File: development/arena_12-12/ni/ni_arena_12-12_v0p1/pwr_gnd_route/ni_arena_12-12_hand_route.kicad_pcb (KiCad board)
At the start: 6 copper layers, 228.6 x 228.6 mm, 581 parts, among them J1 Barrel_Jack, J2 NI_TE_68pos, J3 Barrel_Jack, P1 CONN15, P10 CONN15, P11 CONN15, P12 CONN15, P2 CONN15, P3 CONN15, P4 CONN15, P5 CONN15, P6 CONN15, P7 CONN15, P8 CONN15, P9 CONN15, Q1 MOSFET_NCHAN, SW1 SW_SPDT, U1 AP2112K-3.3, U10 TXB0108PW, U100 74LVC2G17, U101 74LVC2G17, U102 74LVC2G17, U103 74LVC2G17, U104 74LVC2G17, U105 74LVC2G17, U106 74LVC2G17, U107 74LVC2G17, U108 74LVC2G17, U109 74LVC2G17, U11 TXB0108PW, U110 74LVC2G17, U12 TXB0108PW, U13 TXB0108PW, U14 TXB0108PW, U15 TXB0108PW, U16 TXB0108PW, U17 TXB0108PW, U18 TXB0108PW, U19 74LVC2G17, U2 TXB0108PW, U20 74LVC2G17, U21 74LVC2G17, U22 74LVC2G17, U23 74LVC2G17, U24 74LVC2G17, U25 74LVC2G17, U26 74LVC2G17, U27 74LVC2G17, U28 74LVC2G17, U29 74LVC2G17, U3 TXB0108PW, U30 74LVC2G17, U31 74LVC2G17, U32 74LVC2G17, U33 74LVC2G17, U34 74LVC2G17, U35 74LVC2G17, U36 74LVC2G17, U37 74LVC2G17, U38 74LVC2G17, U39 74LVC2G17, U4 TXB0108PW, U40 74LVC2G17, U41 74LVC2G17, U42 74LVC2G17, U43 74LVC2G17, U44 74LVC2G17, U45 74LVC2G17, U46 74LVC2G17, U47 74LVC2G17, U48 74LVC2G17, U49 74LVC2G17, U5 TXB0108PW, U50 74LVC2G17, U51 74LVC2G17, U52 74LVC2G17, U53 74LVC2G17, U54 74LVC2G17, U55 74LVC2G17, U56 74LVC2G17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

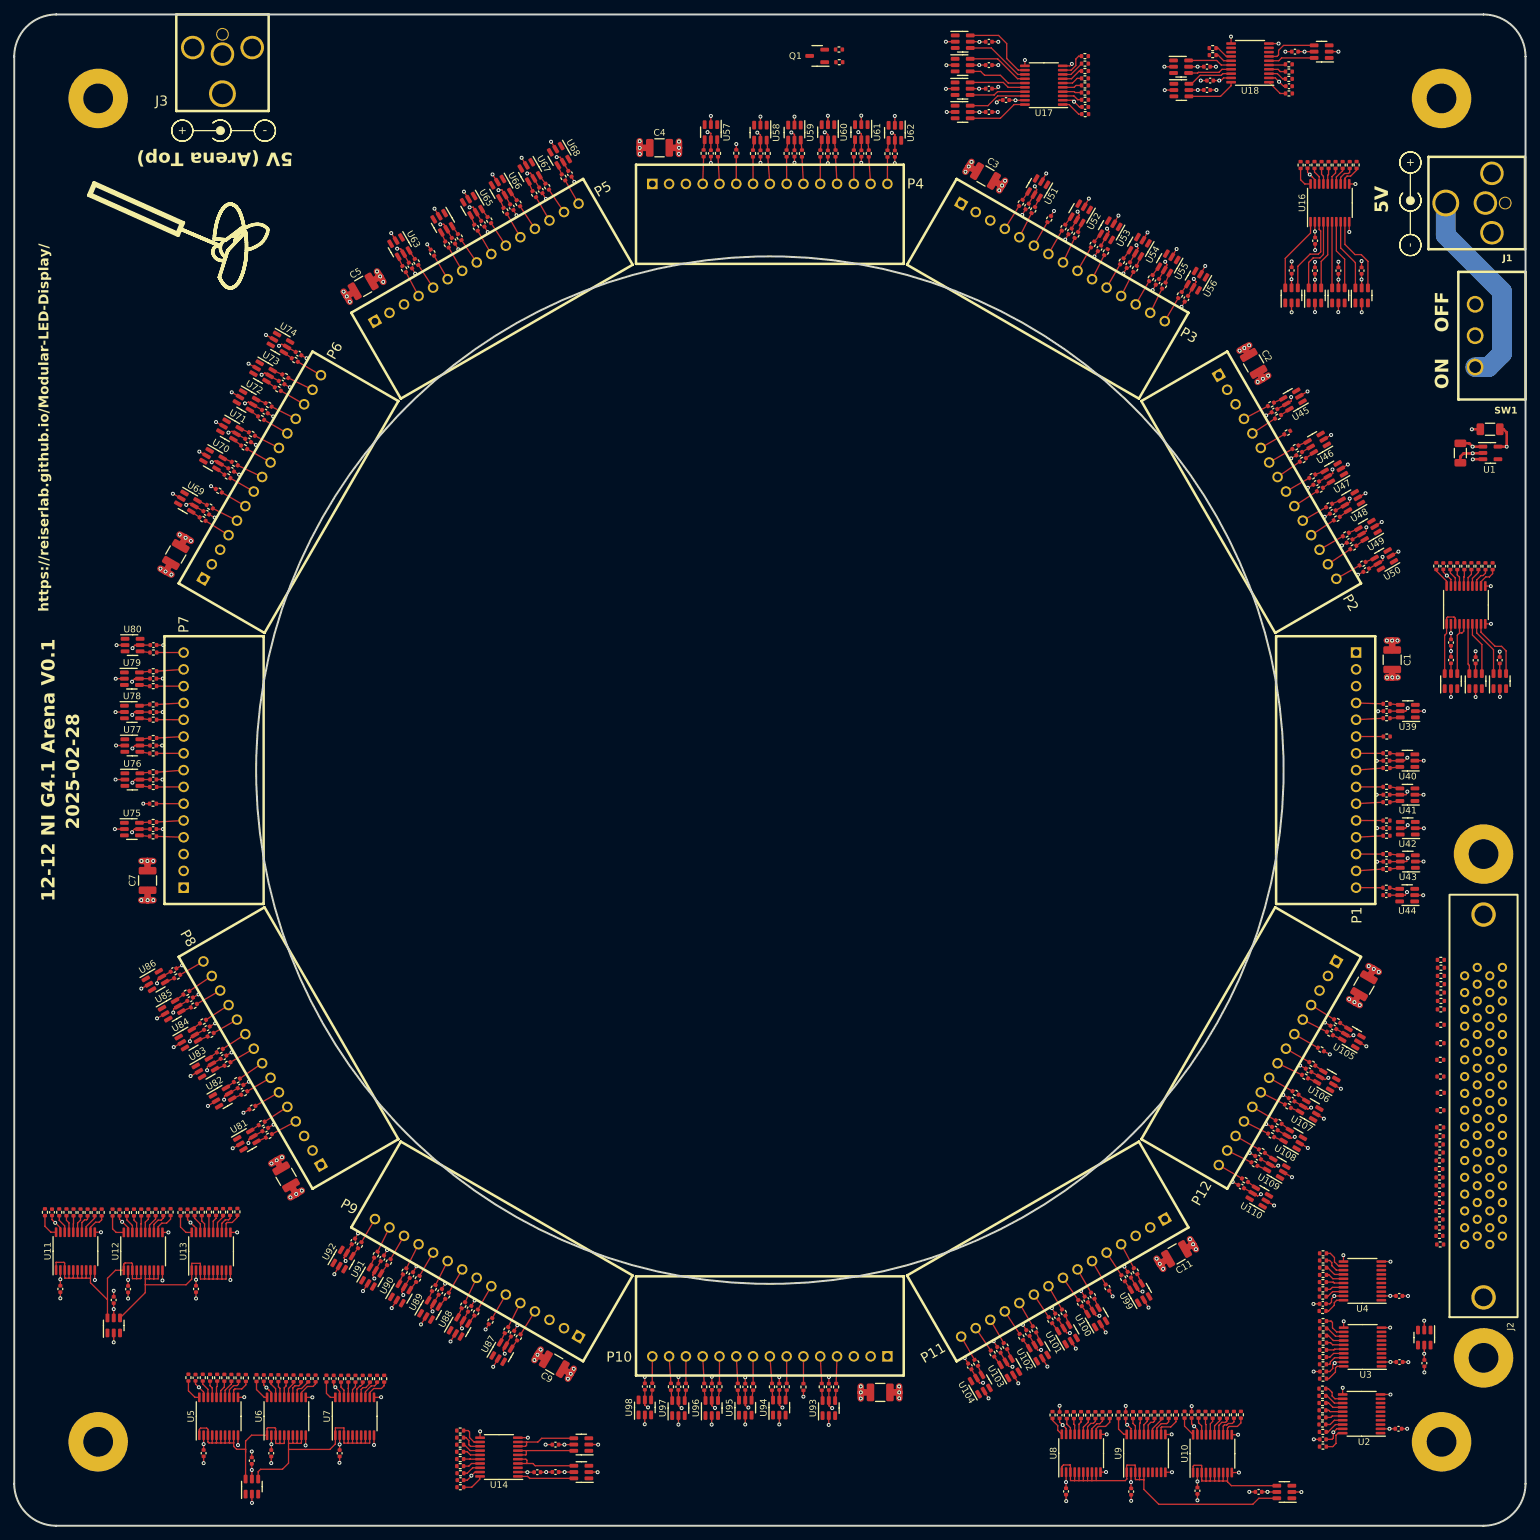
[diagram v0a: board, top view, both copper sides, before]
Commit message: Finished autorouting for new route of NI 12-12 arena which fix hand route.
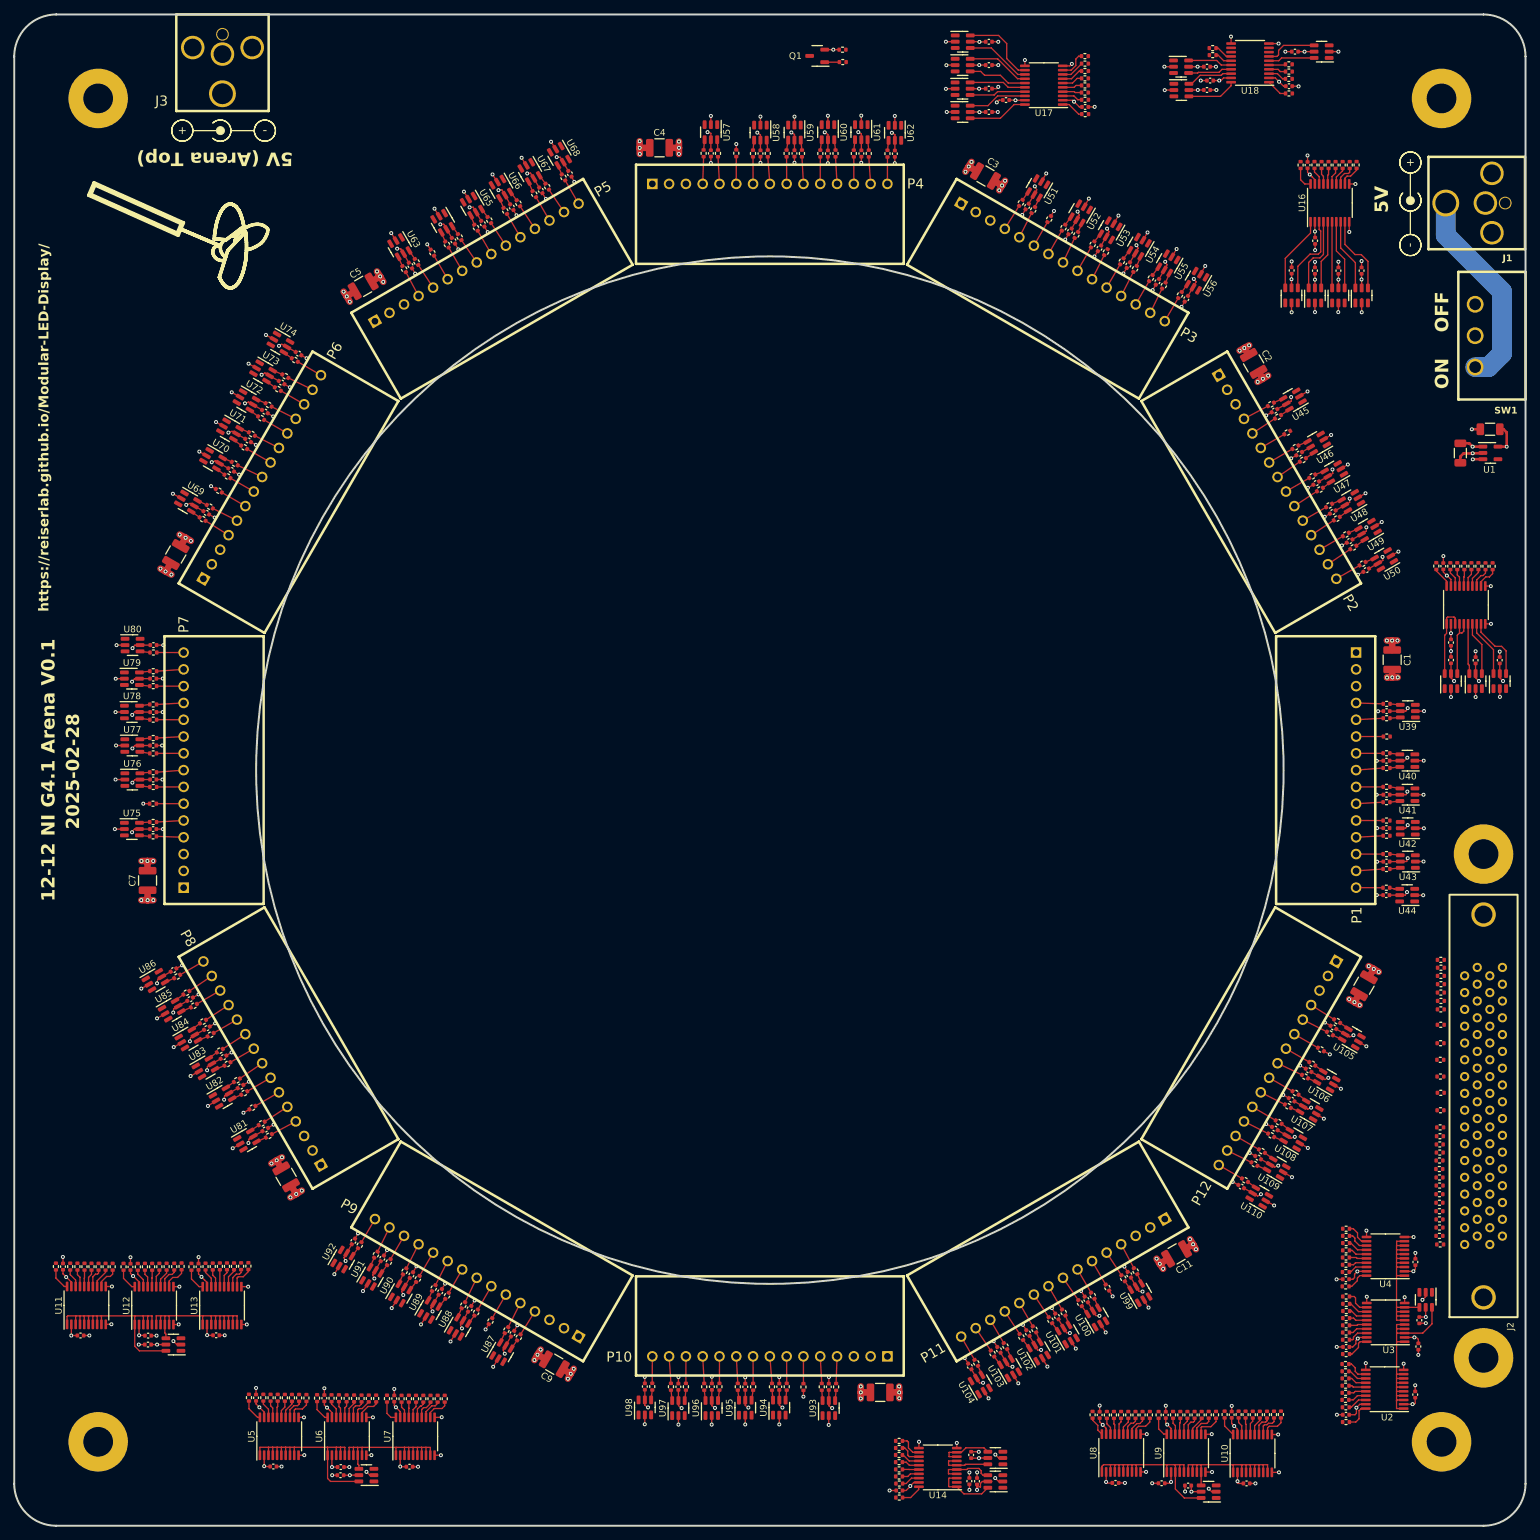
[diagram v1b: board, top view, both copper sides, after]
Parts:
- moved R125 66.4 mm to (197.4, 287.8)
- moved R129 66.4 mm to (197.3, 282.5)
- moved R130 66.4 mm to (197.3, 281.4)
- moved U14 66.4 mm to (203.2, 283.3)
- moved C132 66.4 mm to (197.4, 286.8)
- moved R126 66.4 mm to (197.4, 285.7)
- moved R127 66.4 mm to (197.3, 284.6)
- moved R128 66.4 mm to (197.3, 283.6)
- moved R131 66.4 mm to (197.3, 280.3)
- moved R132 66.4 mm to (197.3, 279.3)
- moved C131 65.4 mm to (208.0, 285.3), turned to 90 degrees
- moved C19 63.8 mm to (209.1, 285.4), turned to 90 degrees
- moved C20 62.9 mm to (208.2, 281.4), turned to 90 degrees
- moved U24 62.7 mm to (211.9, 281.9)
- moved U23 62.6 mm to (211.9, 285.4)
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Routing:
- net Net-(U2-A1): track 0.00 -> 33.5 mm
- net Net-(U3-A5): track 0.00 -> 28.5 mm
- net Net-(U8-A1): track 52.9 -> 32.5 mm
- net GND: track 297.2 -> 309.8 mm, vias 259 -> 273
- net Net-(U6-A5): track 40.6 -> 28.8 mm
- net Net-(U12-A5): track 40.0 -> 30.3 mm
- net Net-(U10-A1): track 24.1 -> 27.7 mm
- net Net-(U14-A5): track 10.3 -> 7.93 mm
- net Net-(U14-A7): track 10.6 -> 8.20 mm
- net Net-(Q1-G): track 0.00 -> 2.23 mm
- net +3.3V: track 98.5 -> 100.5 mm, vias 46 -> 49
- net Net-(U14-A3): track 10.5 -> 8.58 mm
- net Net-(U11-A1): track 37.8 -> 36.6 mm
- net Net-(U14-A1): track 8.61 -> 9.20 mm

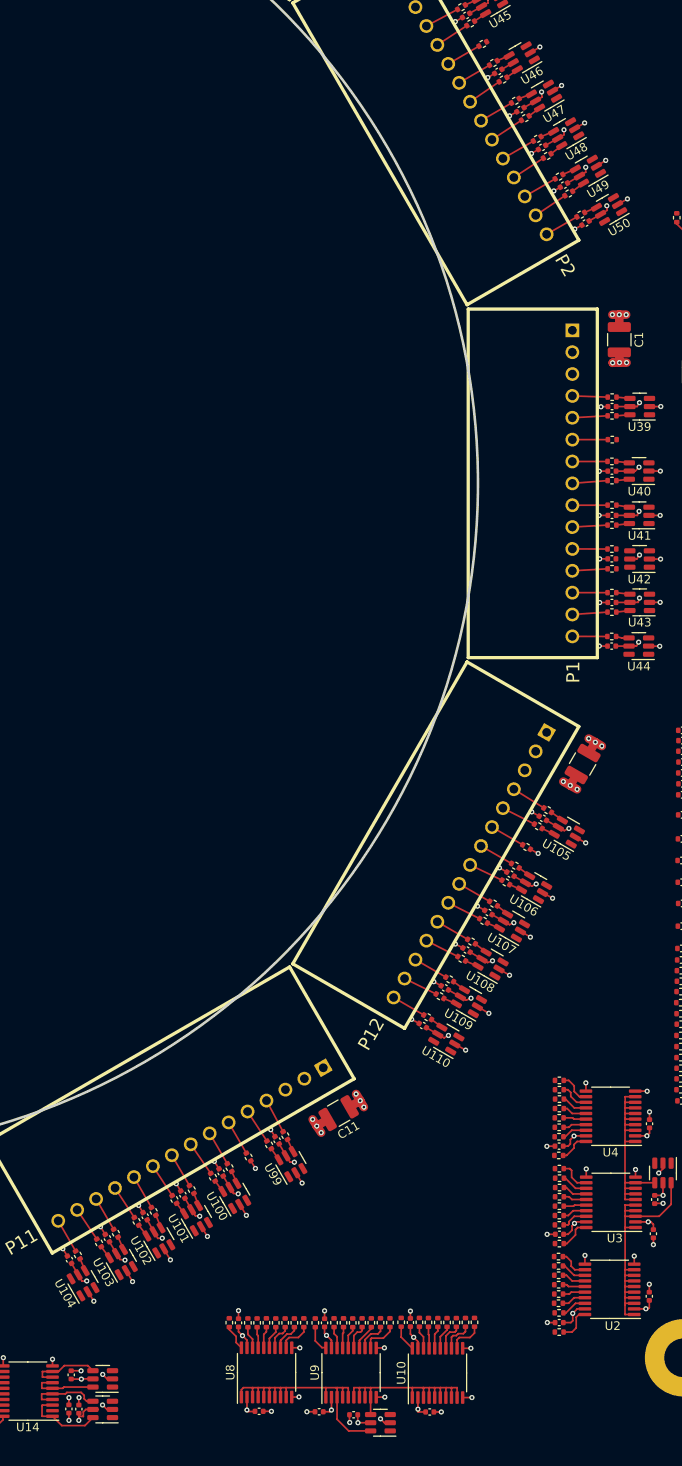
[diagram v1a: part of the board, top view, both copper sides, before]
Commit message: Add new route to NI 12-12 .kicad_pcb file.
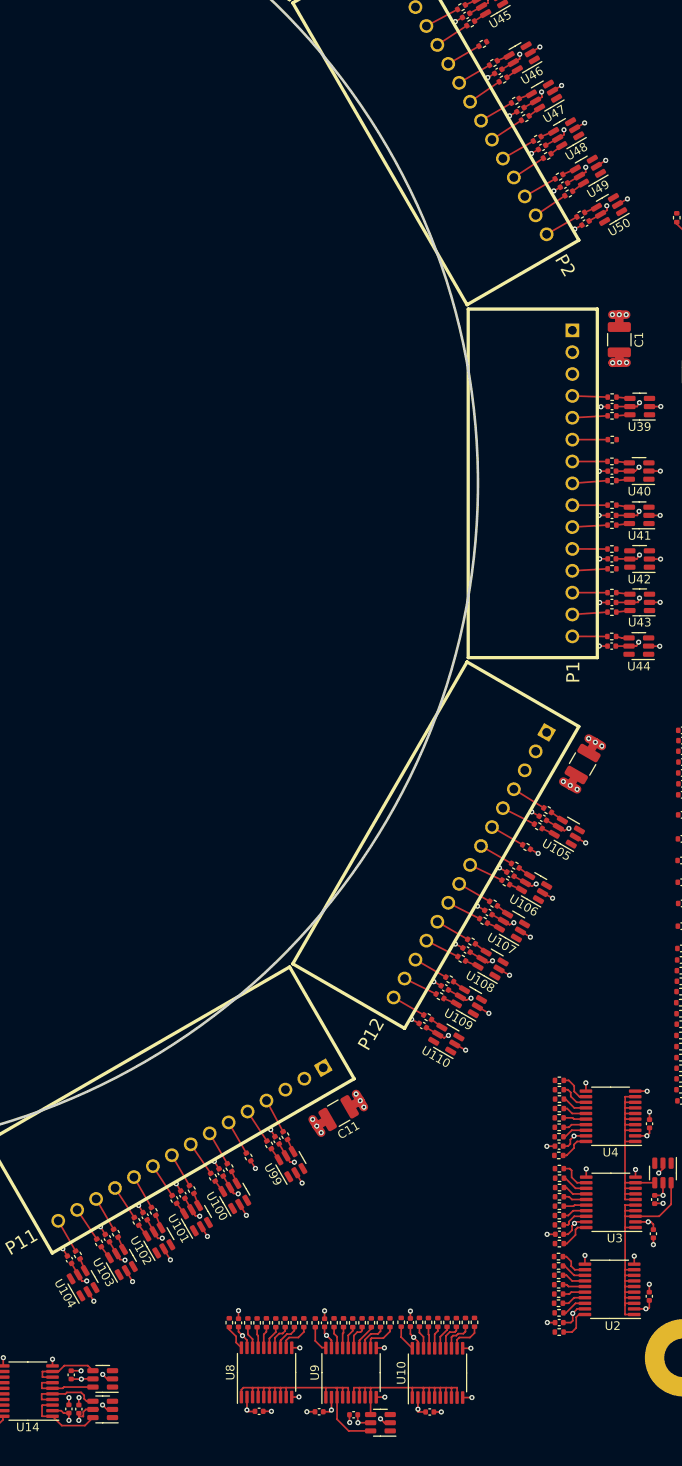
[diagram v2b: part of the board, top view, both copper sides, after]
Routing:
- net +5V: track 319.4 -> 322.4 mm, vias 132 -> 133
- net +3.3V: track 100.5 -> 102.5 mm
